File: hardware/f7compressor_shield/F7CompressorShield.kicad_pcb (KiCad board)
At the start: 2 copper layers, 191.2 x 182.7 mm, 24 parts, among them CN10 PinSocket_2x17_P2.54mm_Vertic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, CN11 PinSocket_2x35_P2.54mm_Vertic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, CN12 PinSocket_2x35_P2.54mm_Vertic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, CN7 PinSocket_2x10_P2.54mm_Vertic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, CN8 PinSocket_2x08_P2.54mm_Vertic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, CN9 PinSocket_2x15_P2.54mm_Vertic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, J1 PinSocket_2x17_P2.54mm_Vertic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, J2 PinHeader_1x06_P2.54mm_Vertic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, J5 TerminalBlock_MaiXu_MX126-5.0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, J6 TerminalBlock_MaiXu_MX126-5.0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

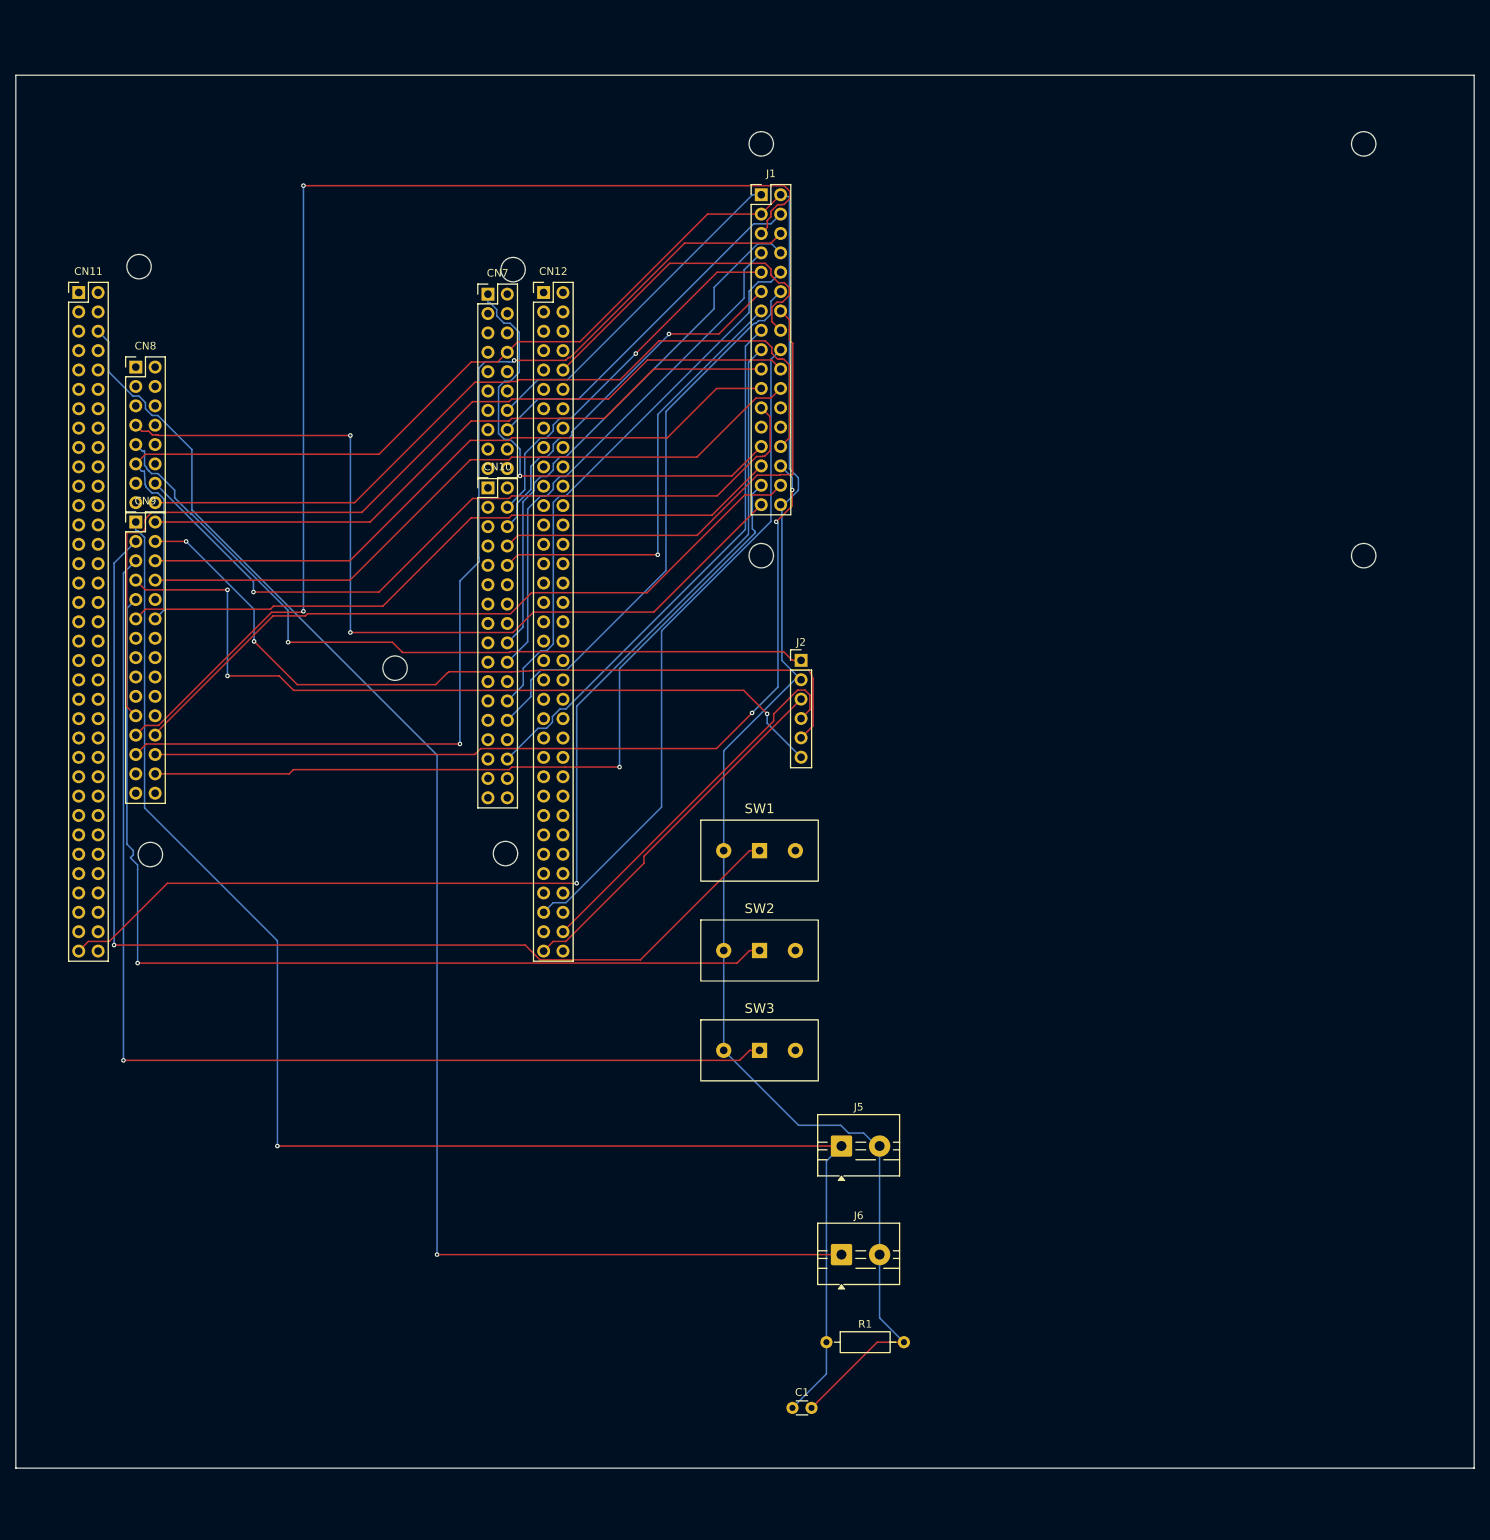
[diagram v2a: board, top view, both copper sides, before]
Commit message: Fix J1 LCD header pin 1/3 swap; correct wiring_diagram.html to match
Checked J1 against the LCD module's own manufacturer schematic
(read pin-by-pin via exact PDF text coordinates) and found pin 1 is
DC-5V (required power), not FMC_D0 -- the data bus actually starts
at pin 3, which this project (and wiring_diagram.html) had as GND.
Every other pin (4-34) already matched the real schematic exactly,
so this was isolated to the first two positions. Confirmed nothing
is physically wired to the LCD yet, so this never reached hardware.

Fixed J1's net assignment (pin1->+5V, pin3->FMC_D0) and the same
error in wiring_diagram.html, which previously didn't document the
LCD's real 5V power pin at all.

Re-routed after the pin change. One new clearance violation (a
BL_CTRL via packed in with CN12 pads and 5 other FMC nets) had no
valid position for a standard 0.6mm via anywhere within 0.8mm -- an
attempted F.Cu-only reroute around it looked clean until DRC caught
a true segment crossing my distance-based checker had missed (fixed
the checker, but the simpler and correct fix was just shrinking both
vias to 0.5mm, the board's declared minimum, at their original
positions).

ERC clean, DRC 0 unconnected / 0 clearance violations.

Co-Authored-By: Claude Sonnet 5 <noreply@anthropic.com>
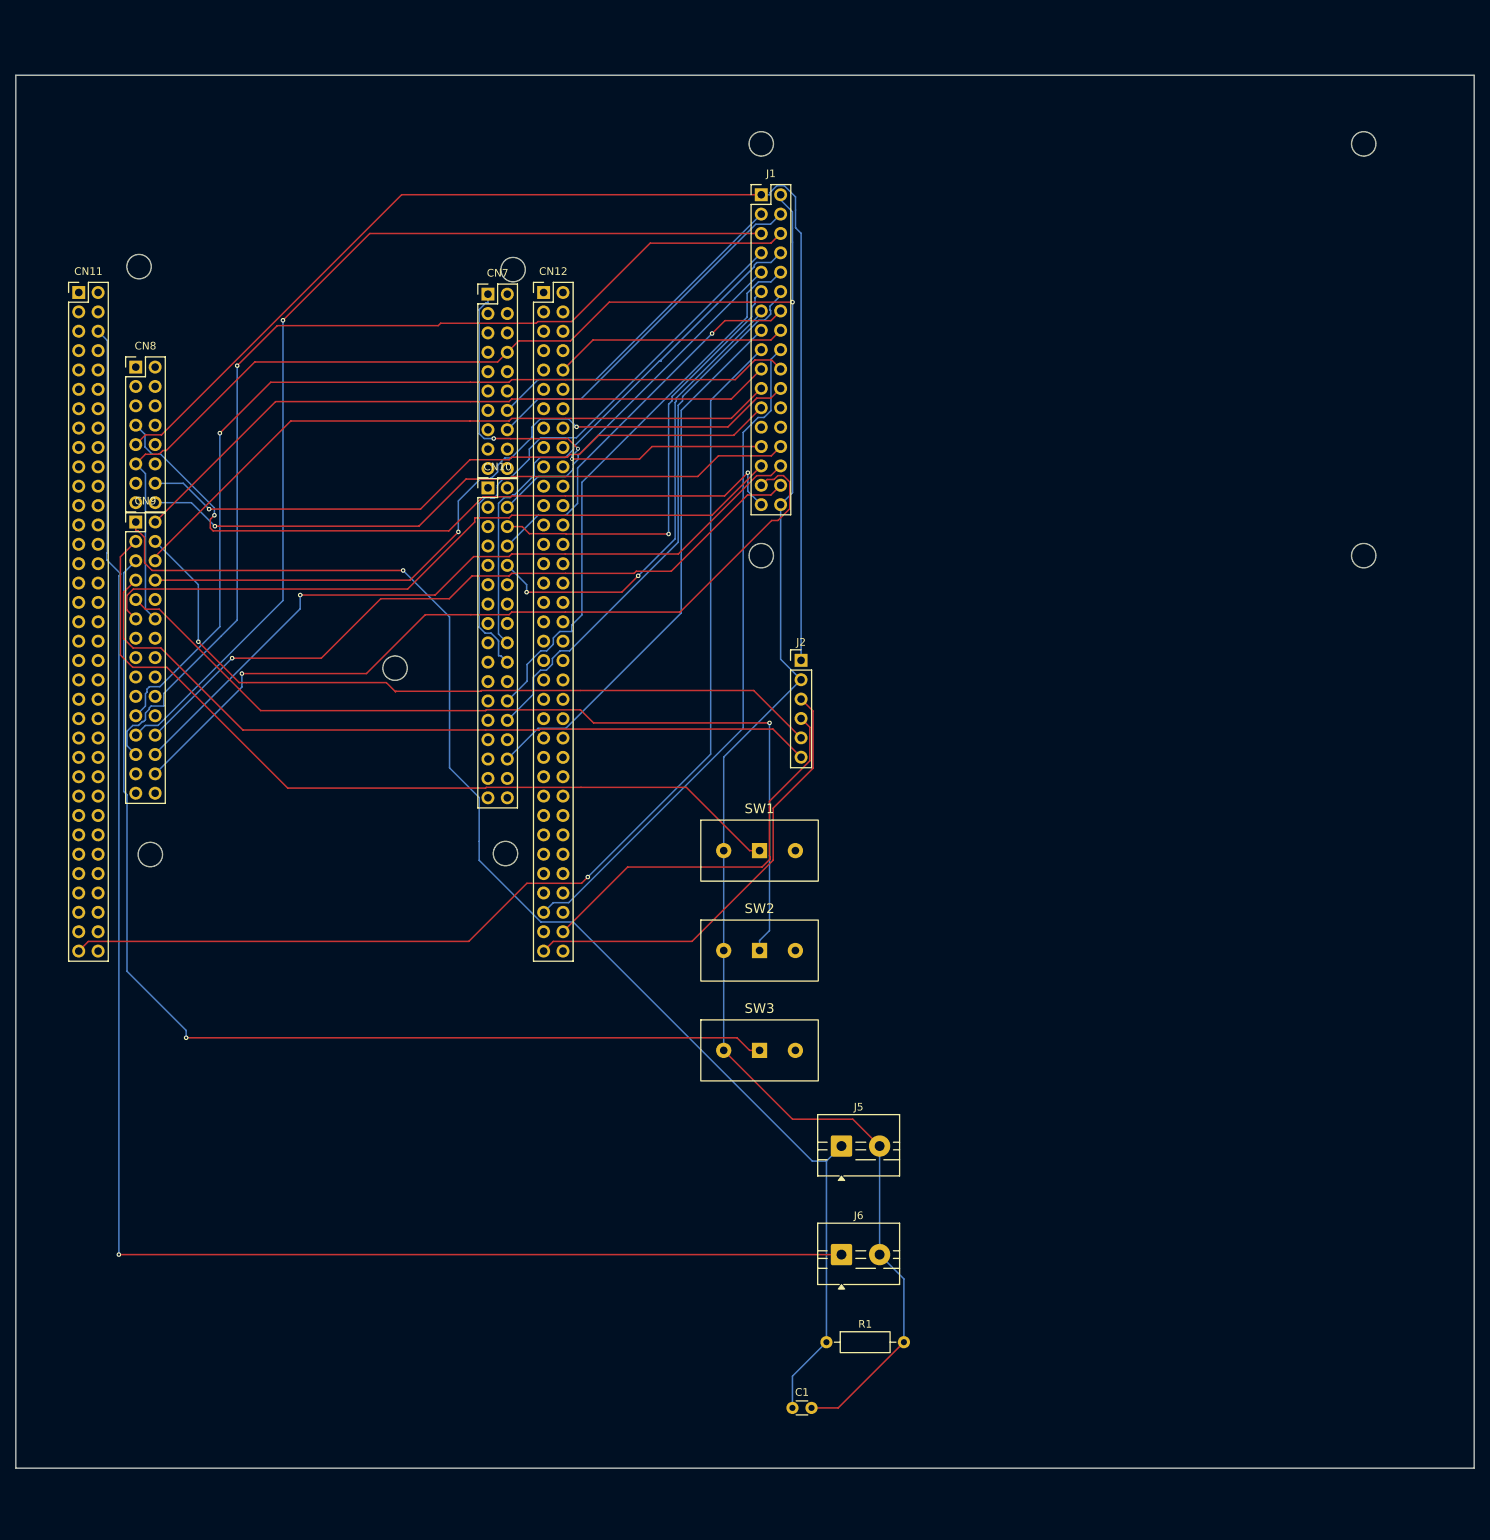
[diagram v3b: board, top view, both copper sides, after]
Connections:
- J1 pad 1: FMC_D0 -> +5V
- J1 pad 3: GND -> FMC_D0
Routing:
- net +5V: track 103.3 -> 162.4 mm, vias 1 -> 0
- net OIL_SW: track 145.5 -> 110.3 mm, vias 1 -> 0
- net FMC_D2: track 156.2 -> 130.8 mm, vias 2 -> 1
- net +5V_IN: track 193.4 -> 217.2 mm
- net PRESSURE_SENSE: track 200.7 -> 181.3 mm
- net +3V3: track 115.4 -> 97.4 mm
- net TP_IRQ: track 104.9 -> 87.6 mm, vias 0 -> 1
- net TP_SCK: track 115.9 -> 98.8 mm, vias 3 -> 1
- net LCD_RST: track 101.1 -> 86.4 mm
- net FMC_D13: track 44.7 -> 30.7 mm
- net FMC_D11: track 63.4 -> 51.3 mm, vias 0 -> 1
- net ESTOP: track 131.3 -> 120.3 mm
- net RELAY_RUN: track 48.0 -> 59.0 mm
- net FMC_D8: track 49.7 -> 58.4 mm
- net GND: track 311.2 -> 303.5 mm, vias 0 -> 1
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
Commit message: Use real part numbers for J5/J6 and SW1-3; add generic switch 3D model
J5 and J6 now both use the exact KiCad-bundled footprint for Phoenix
Contact 1727010 (MKDS 1/2-3,81), replacing the generic MX126 placeholder.
SW1-3 updated to the real part, Dailywell 1MS1T1B1M1QES-5 -- confirmed
pin spacing (4.70mm) already matched the existing custom footprint
exactly. Its 6.35mm mounting bushing is nearly as wide as the whole
switch body, so it was left off the PCB footprint (strong evidence it
mounts through an enclosure panel, not the board).

Added a generic placeholder 3D model (3dmodels/SW_MTS1_generic.wrl) for
the switches, sized to the real part's body envelope, since no bundled
or downloadable model exists. Found and fixed a real scaling bug while
attaching it: KiCad interprets raw VRML coordinates at a fixed 2.54
scale (mm per 0.1in) regardless of the file's actual units. The correct
factor (1/2.54) was found by pixel-measuring the rendered model against
the footprint's own known pad pitch, not guessed -- an initial attempt
using the inches-to-mm factor (1/25.4) undershot by 10x.

Re-routed after both changes. ERC clean, DRC 0 unconnected / 0 clearance
violations.

Co-Authored-By: Claude Sonnet 5 <noreply@anthropic.com>
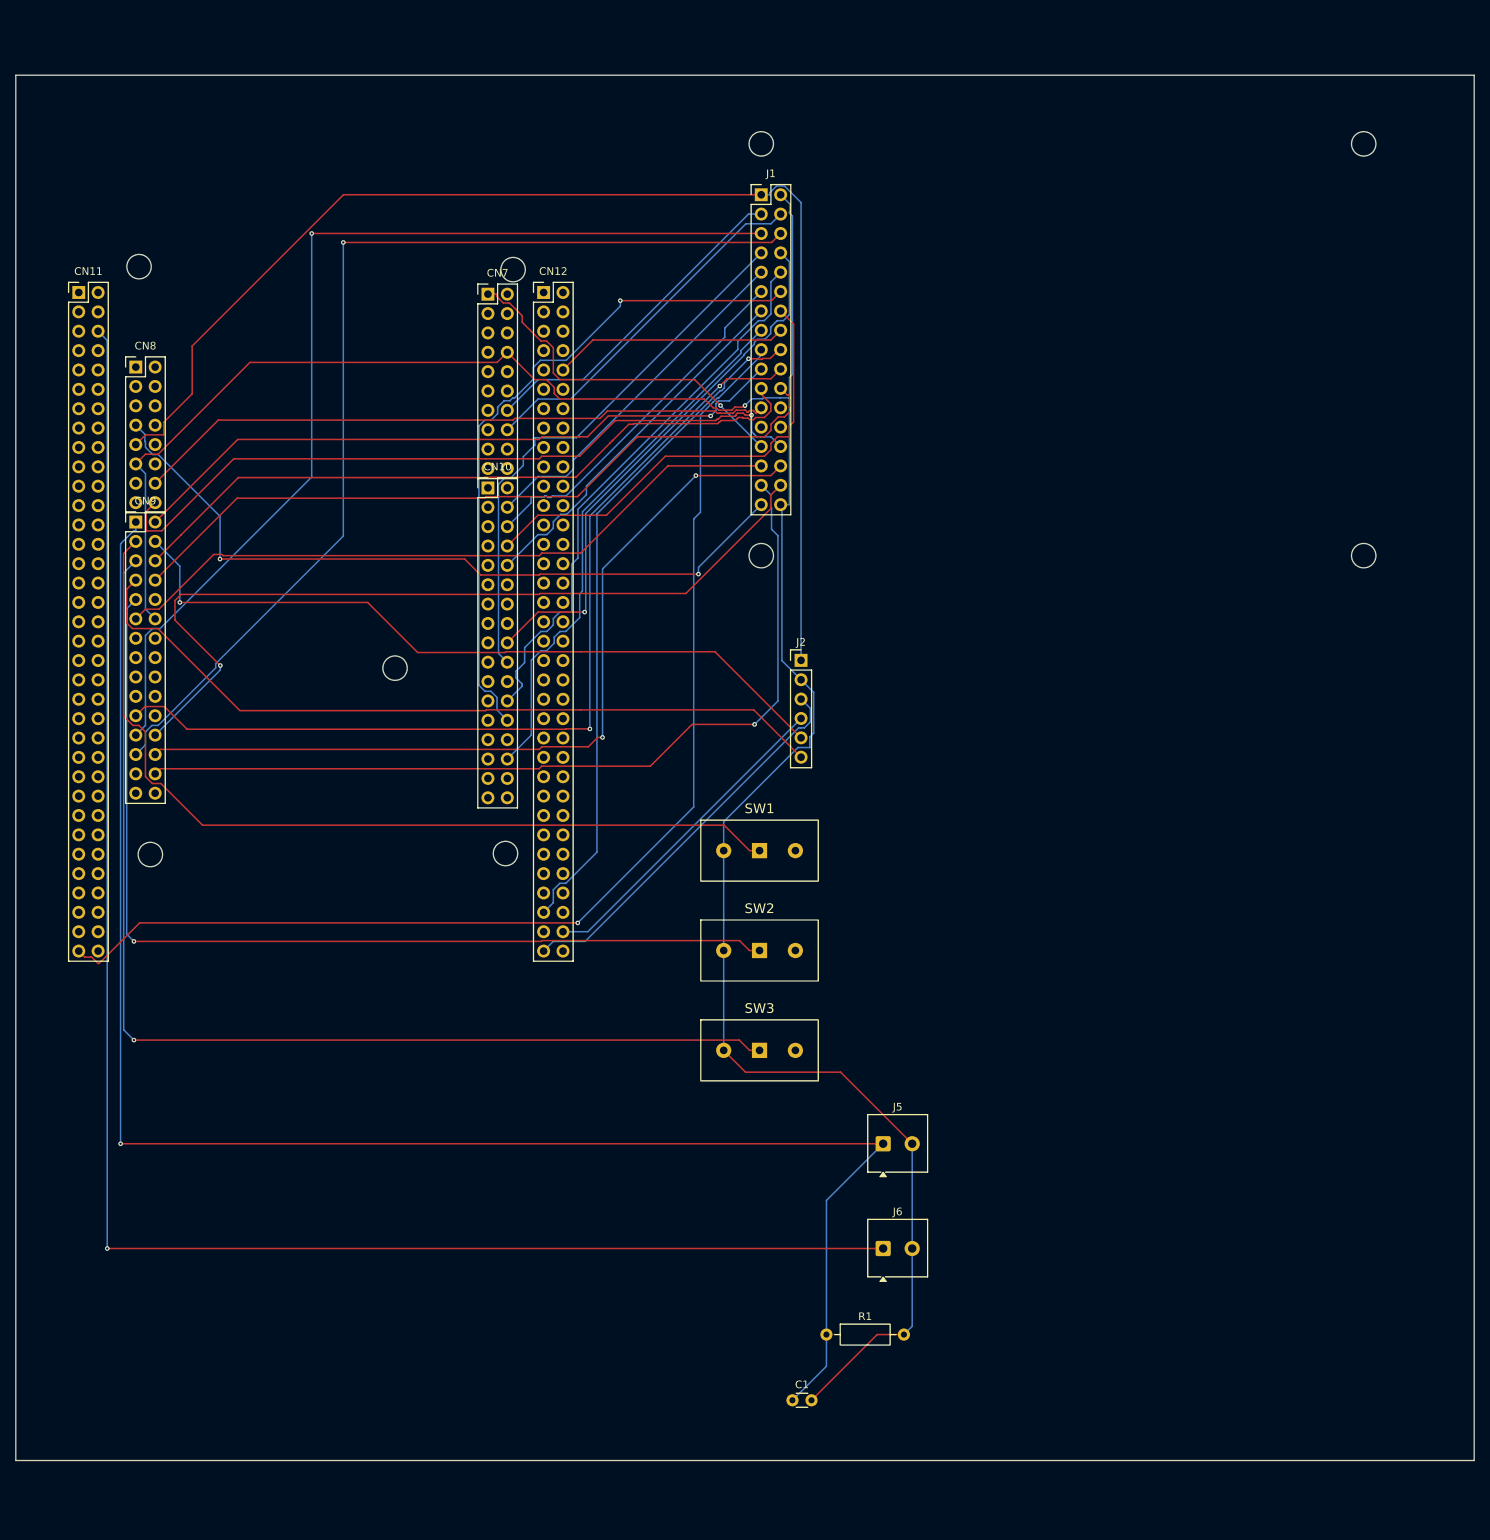
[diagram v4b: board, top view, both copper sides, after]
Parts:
- J5, J6: value TerminalBlock_MaiXu_MX126-5.0-02P_1x02_P5.00mm -> TerminalBlock_Phoenix_MKDS-1-2-3.81_1x02_P3.81mm_Horizontal; footprint TerminalBlock_MaiXu_MX126-5.0-02P_1x02_P5.00mm -> TerminalBlock_Phoenix_MKDS-1-2-3.81_1x02_P3.81mm_Horizontal
- moved J6 5.52 mm to (113.7, 153.9)
- moved J5 5.47 mm to (113.7, 140.1)
- moved C1 1.00 mm to (101.8, 173.8)
- moved R1 1.00 mm to (106.3, 165.1)
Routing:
- net PRESSURE_SENSE: track 181.3 -> 221.1 mm
- net FMC_D9: track 72.8 -> 89.3 mm, vias 0 -> 1
- net TP_SDO: track 95.6 -> 110.4 mm
- net FMC_D10: track 61.5 -> 48.3 mm, vias 2 -> 0
- net BL_CTRL: track 59.9 -> 46.8 mm, vias 3 -> 1
- net TP_SCK: track 98.8 -> 110.6 mm, vias 1 -> 2
- net FMC_D8: track 58.4 -> 47.4 mm, vias 1 -> 0
- net FMC_D11: track 51.3 -> 60.9 mm, vias 1 -> 0
- net RELAY_IN2: track 52.2 -> 42.8 mm
- net TP_IRQ: track 87.6 -> 96.9 mm
- net ESTOP: track 120.3 -> 128.3 mm
- net TP_SDI: track 106.8 -> 114.8 mm
- net RELAY_RUN: track 59.0 -> 50.9 mm
- net OIL_SW: track 110.3 -> 117.7 mm
- net GND: track 303.5 -> 310.3 mm
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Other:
- board size 191.2 x 182.7 mm -> 191.2 x 181.7 mm
